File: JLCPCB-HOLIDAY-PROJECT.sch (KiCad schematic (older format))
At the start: 67 parts, among them J1 USB_A_PCB, U1 CH340G, U2 STM32F030F4P6, U3 AP1117-3v3, Y1 12mhz-Crystal_GND24, Y2 12mhz-Crystal_GND24

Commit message: Sync
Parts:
- added 5V-IN1: Conn_01x02_Male, Connector_PinHeader_2.54mm:PinHeader_1x02_P2.54mm_Vertical, symbol Connector:Conn_01x02_Male
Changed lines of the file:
@@
 Text GLabel 1340 3370 2    50   Input ~ 0
 UART_RX
+$Comp
+L Connector:Conn_01x02_Male 5V-IN1
+U 1 1 5FA7B0BD
+P 2280 3120
+F 0 "5V-IN1" H 2388 3301 50  0000 C CNN
+F 1 "Conn_01x02_Male" H 2388 3210 50  0000 C CNN
+F 2 "Connector_PinHeader_2.54mm:PinHeader_1x02_P2.54mm_Vertical" H 2280 3120 50  0001 C CNN
+F 3 "~" H 2280 3120 50  0001 C CNN
+	1    2280 3120
+	1    0    0    -1
+$EndComp
+Text GLabel 2480 3220 2    50   Input ~ 0
+GND
+Text GLabel 2480 3120 2    50   Input ~ 0
+VBUS
 $EndSCHEMATC

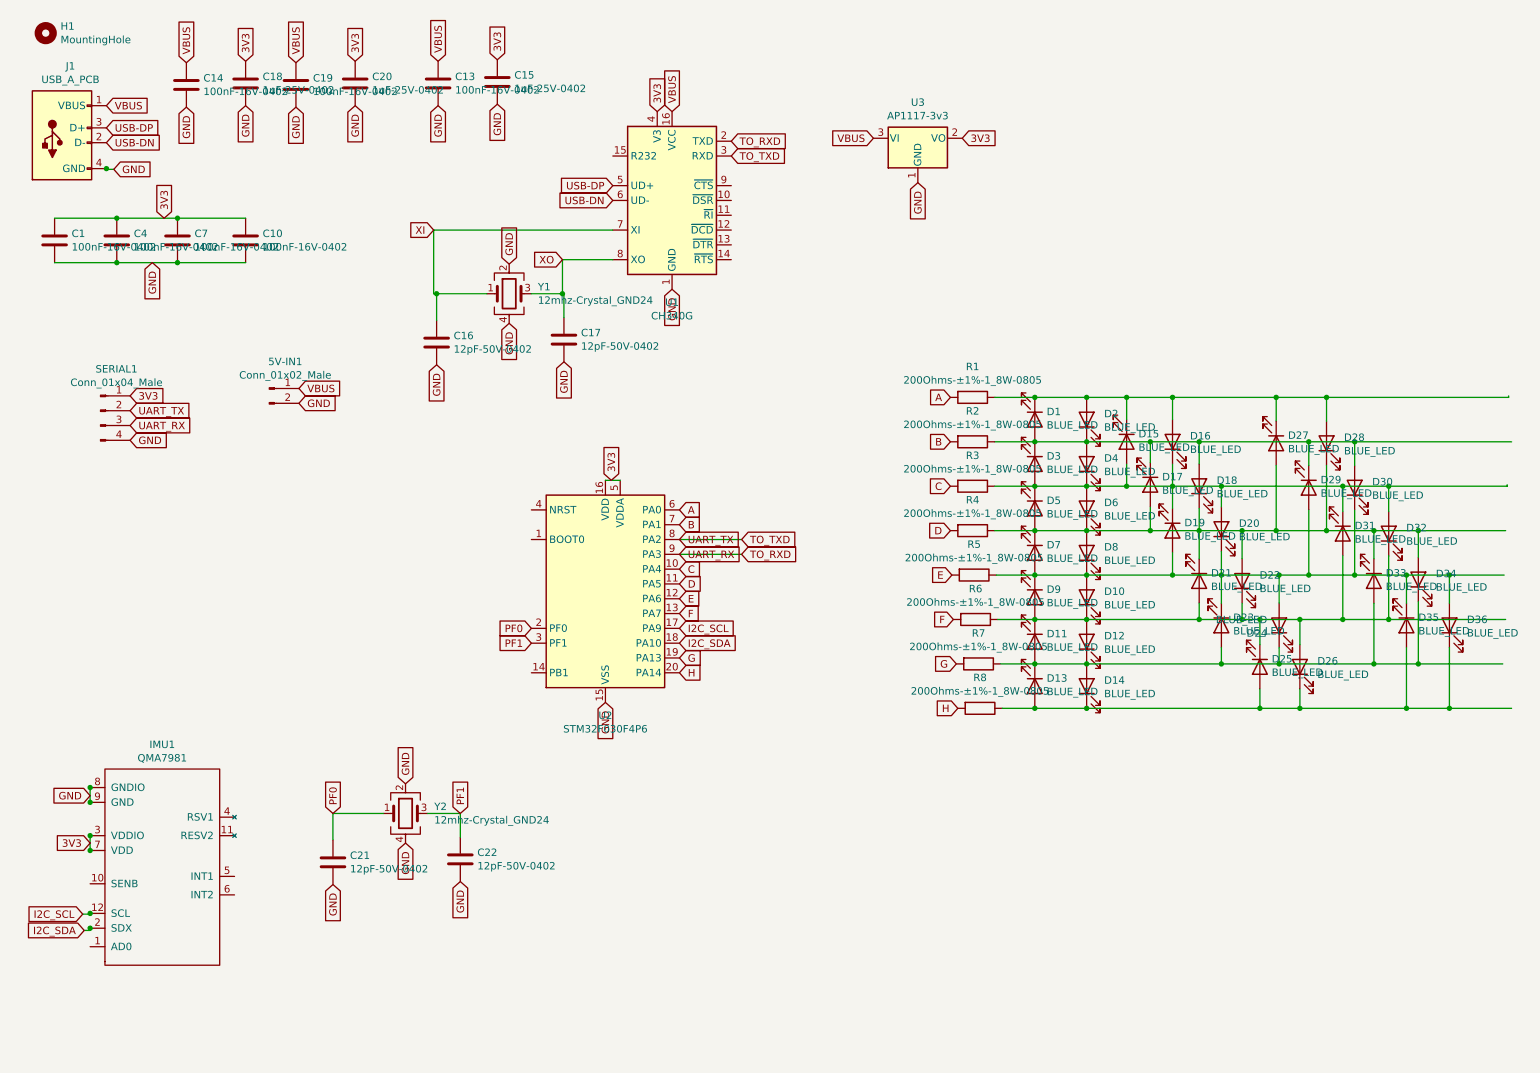
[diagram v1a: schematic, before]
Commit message: Updated traces to add interrupt return, address set to 0, and boot/nrst for the mcu
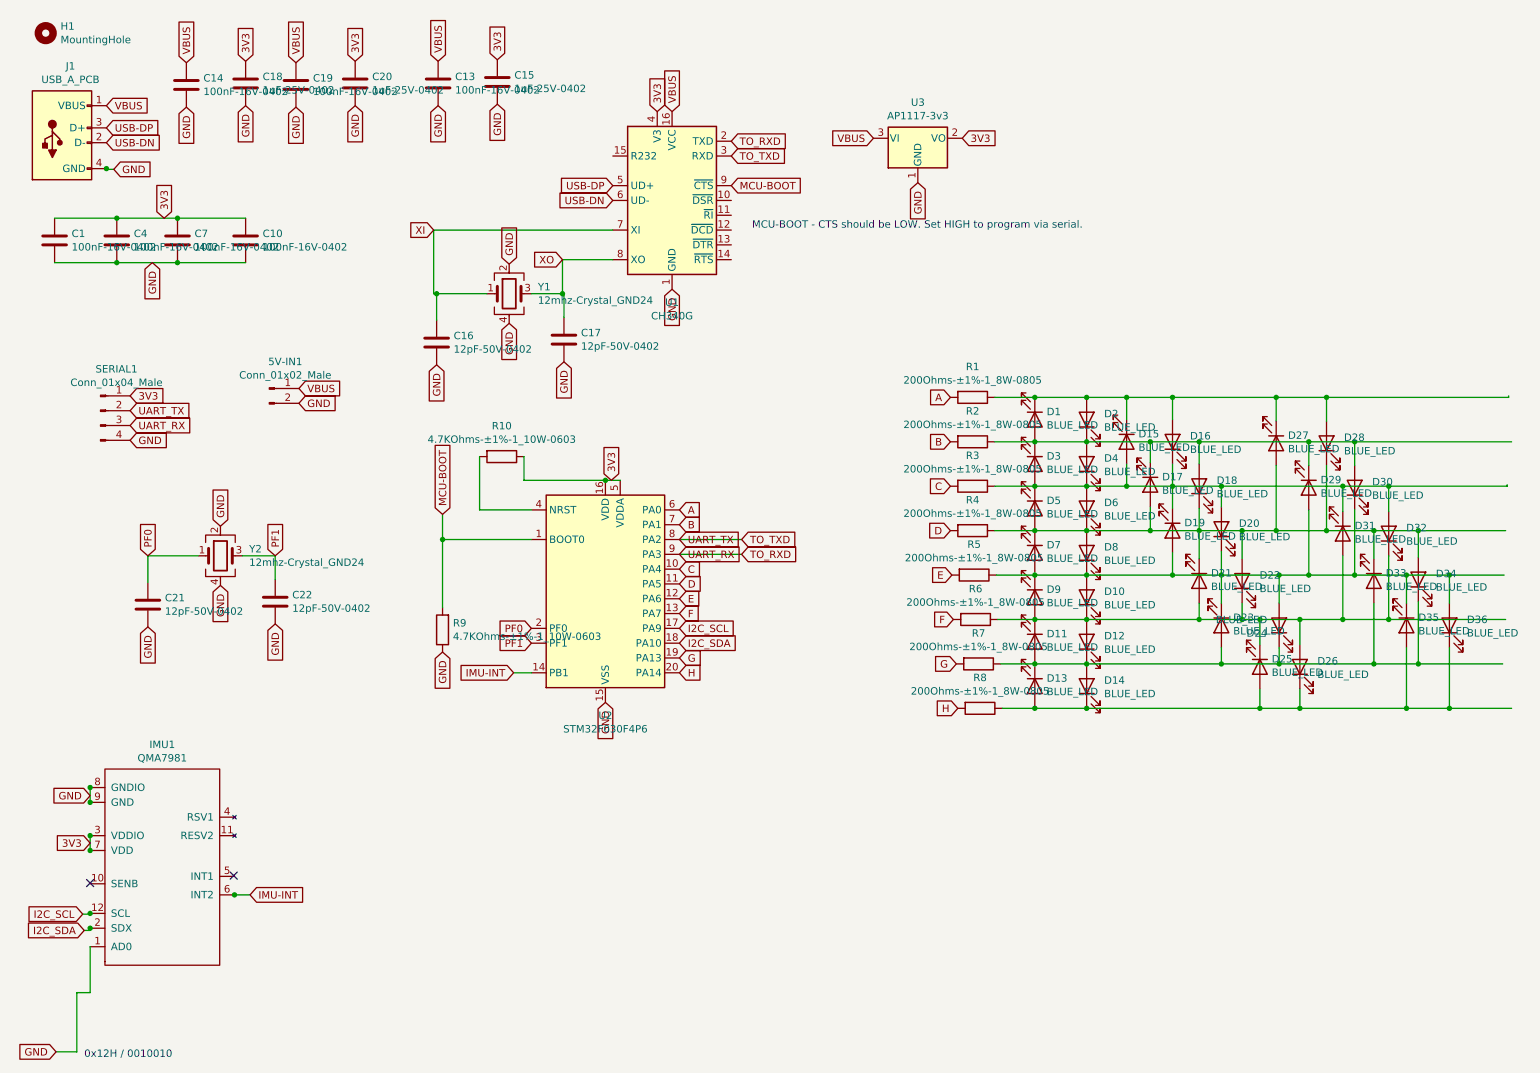
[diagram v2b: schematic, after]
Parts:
- added R10, R9: 4.7KOhms-±1%-1_10W-0603, Resistor_SMD:R_0603_1608Metric, symbol jlcpcb-R:4.7KOhms-±1%-1_10W-0603
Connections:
- net labels added: IMU-INT, MCU-BOOT
- wire segments 149 -> 163
- no-connect marks 0 -> 2
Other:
- note added: "0x12H / 0010010"
- note added: "MCU-BOOT - CTS should be LOW. Set HIGH to program via serial."
- moved on the sheet: C21, C22, Y2
